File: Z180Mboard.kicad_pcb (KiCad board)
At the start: 2 copper layers, 170.2 x 170.2 mm, 66 parts, among them J1 Conn_02x05_Odd_Even, J10 PS2-MINIDIN6-FEMALE-SINGLE, J11 Conn_02x04_Odd_Even, J12 Conn_01x06, J13 Conn_01x06, J14 Conn_02x10_Top_Bottom, J15 Conn_02x05_Odd_Even, J16 DB9_Female, J17 Conn_01x40, J2 Conn_02x05_Odd_Even, J3 Conn_02x05_Odd_Even, J4 Conn_02x05_Odd_Even, J5 Conn_02x05_Odd_Even, J6 Conn_02x05_Odd_Even, J7 Conn_02x05_Odd_Even, J8 Conn_01x08, J9 PS2-MINIDIN6-FEMALE-SINGLE, SW1 SW_SPST, SW2 SW_Push, U1 Z8-L180-S180-180-PLCC-68, U10 74LVC245, U11 DS1307+, U2 SST39SF040, U3 74AHCT138, U4 74AHCT139, U5 AS6C4008-55PCN, U6 AS6C4008-55PCN, U7 82C55A_PLCC, U8 74HCT138, U9 74AHCT151, X1 CXO_DIP8, Y1 Crystal

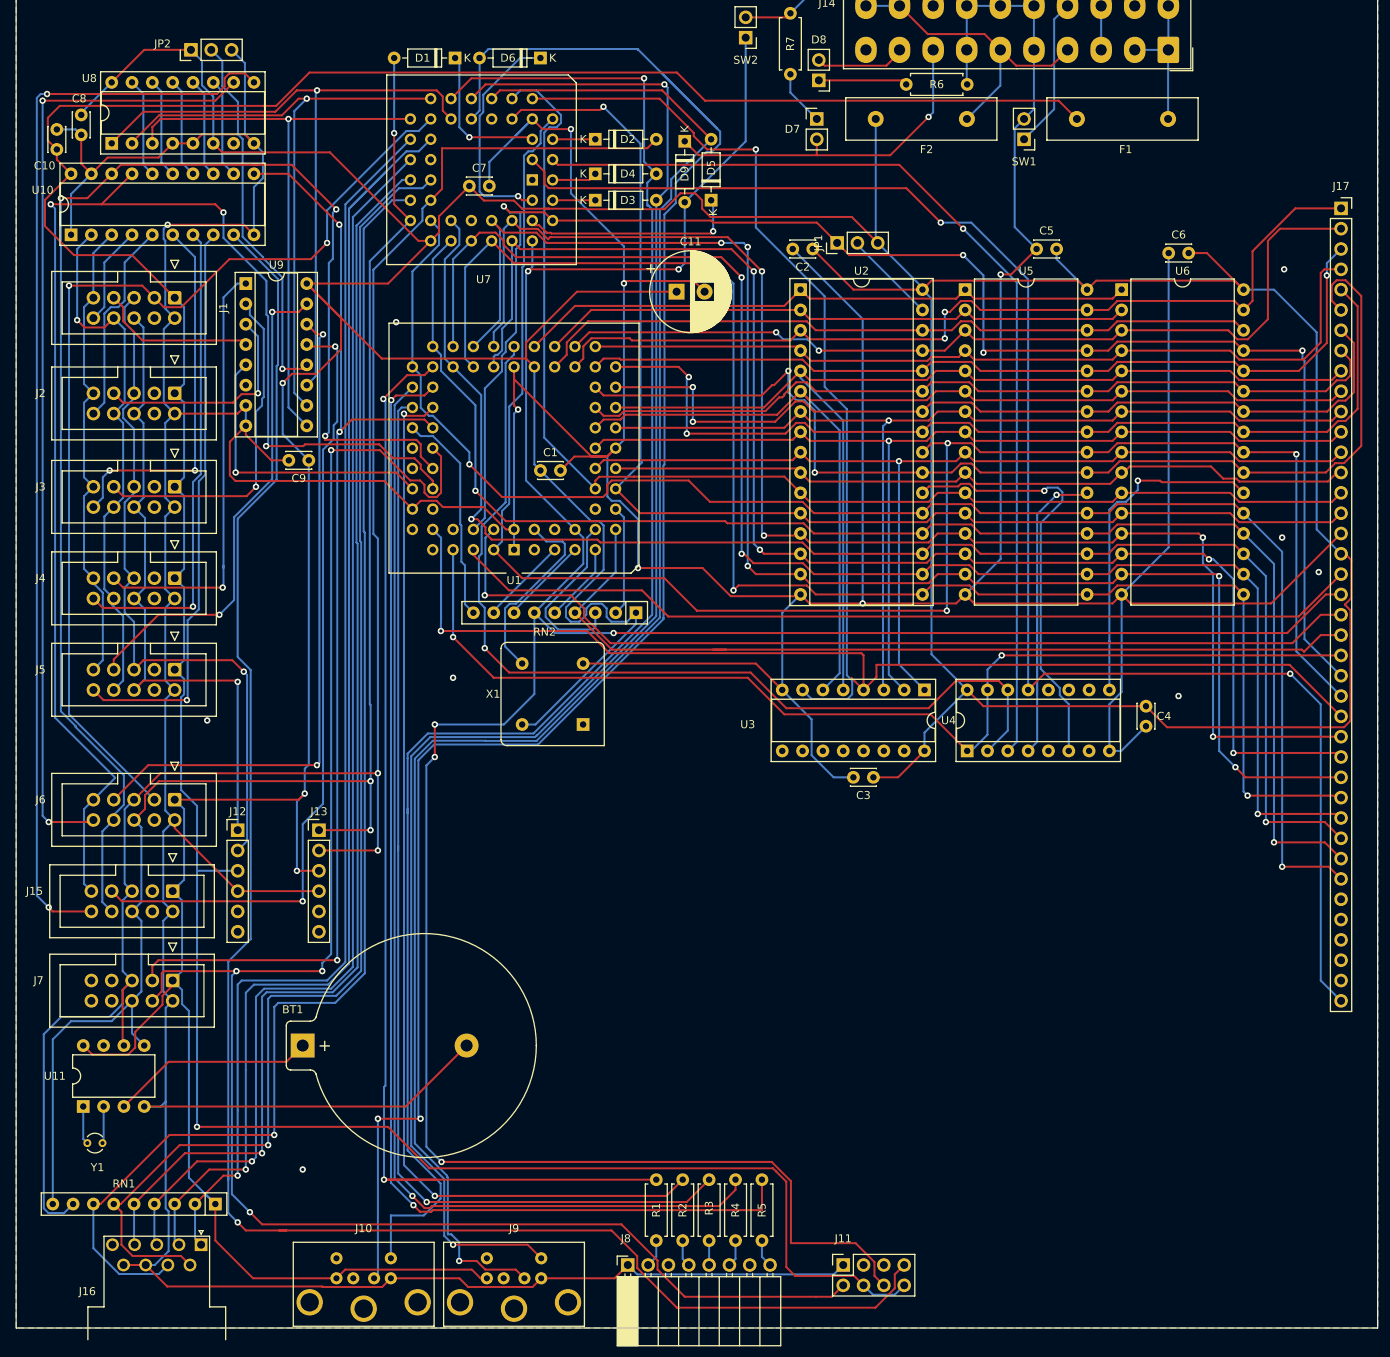
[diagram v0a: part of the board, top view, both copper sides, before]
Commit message: z180mboard: Add the floppy disk interface
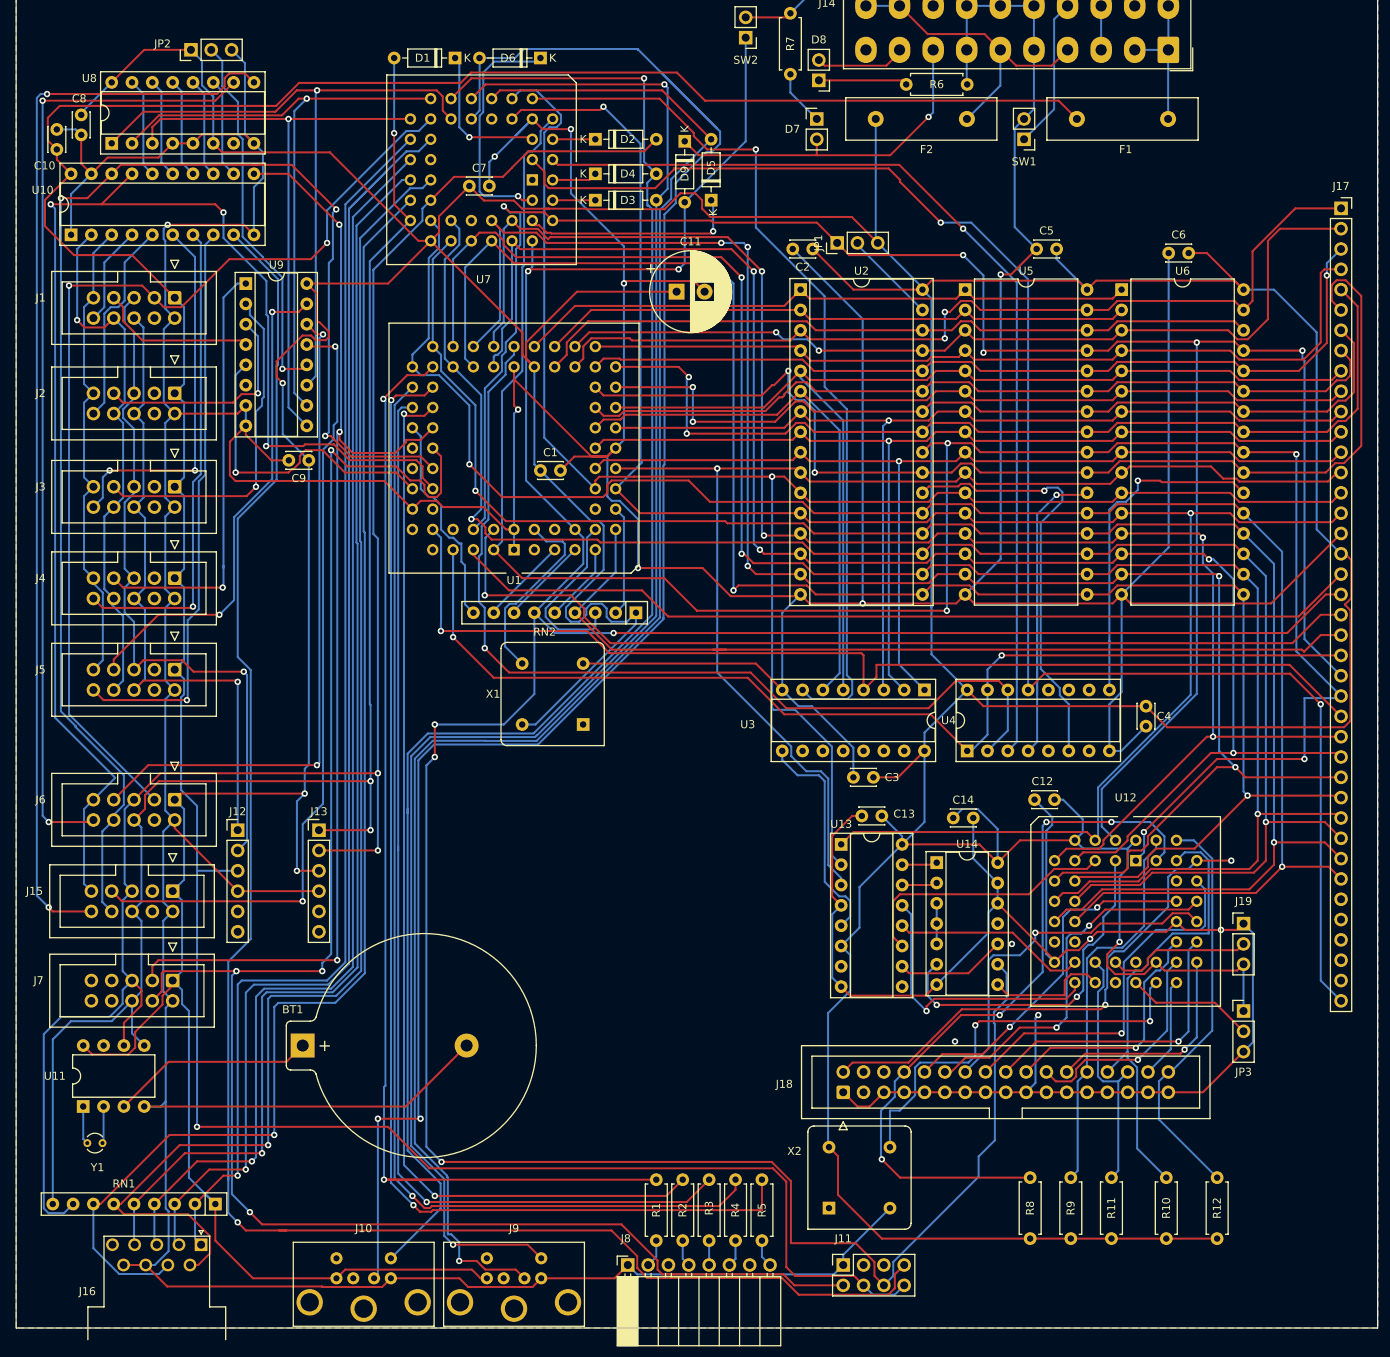
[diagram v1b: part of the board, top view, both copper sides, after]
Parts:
- added C12: 0.1uF, Capacitor_THT:C_Disc_D3.0mm_W2.0mm_P2.50mm, F.Cu at (177.5, 129.3)
- added C13: 0.1uF, Capacitor_THT:C_Disc_D3.0mm_W2.0mm_P2.50mm, F.Cu at (156.0, 131.3)
- added C14: 0.1uF, Capacitor_THT:C_Disc_D3.0mm_W2.0mm_P2.50mm, F.Cu at (164.9, 131.6)
- added J18: Conn_02x17_Odd_Even, Connector_IDC:IDC-Header_2x17_P2.54mm_Vertical, F.Cu at (151.1, 165.9)
- added J19: Conn_01x03, Connector_PinHeader_2.54mm:PinHeader_1x03_P2.54mm_Vertical, F.Cu at (201.2, 144.8)
- added JP3: Jumper_3_Open, Connector_PinHeader_2.54mm:PinHeader_1x03_P2.54mm_Vertical, F.Cu at (201.2, 155.7)
- added R10: 1K, Resistor_THT:R_Axial_DIN0207_L6.3mm_D2.5mm_P7.62mm_Horizontal, F.Cu at (191.5, 184.2)
- added R11: 1K, Resistor_THT:R_Axial_DIN0207_L6.3mm_D2.5mm_P7.62mm_Horizontal, F.Cu at (184.7, 184.2)
- added R12: 1K, Resistor_THT:R_Axial_DIN0207_L6.3mm_D2.5mm_P7.62mm_Horizontal, F.Cu at (197.9, 184.2)
- added R8: 1K, Resistor_THT:R_Axial_DIN0207_L6.3mm_D2.5mm_P7.62mm_Horizontal, F.Cu at (174.5, 184.2)
- added R9: 1K, Resistor_THT:R_Axial_DIN0207_L6.3mm_D2.5mm_P7.62mm_Horizontal, F.Cu at (179.6, 184.2)
- added U12: WD37C65C-DIP44, Package_LCC:PLCC-44_THT-Socket, F.Cu at (187.7, 136.9)
- added U13: 74HCT138, Package_DIP:DIP-16_W7.62mm_Socket, F.Cu at (150.9, 134.9)
- added U14: 74HCT00, Package_DIP:DIP-14_W7.62mm_Socket, F.Cu at (162.8, 137.2)
- added X2: CXO_DIP8, Oscillator:Oscillator_DIP-8, F.Cu at (149.4, 180.3)
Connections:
- U3 pad 9: (no net) -> FDCEN
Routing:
- net GND: track 1000.1 -> 1212.2 mm, vias 15 -> 13
- net VCC: track 769.7 -> 967.7 mm, vias 3 -> 4
- net INDEX: track 0.00 -> 92.3 mm, vias 0 -> 4
- net A0: track 157.9 -> 236.6 mm, vias 1 -> 2
- net WR: track 201.2 -> 269.1 mm, vias 4 -> 5
- net REDWC: track 0.00 -> 65.3 mm, vias 0 -> 2
- net A2: track 94.6 -> 154.1 mm, vias 0 -> 1
- net WPT: track 0.00 -> 57.4 mm
- net A1: track 156.7 -> 210.3 mm, vias 0 -> 1
- net DSKCHG: track 0.00 -> 51.2 mm
- net FDCLK: track 0.00 -> 51.1 mm, vias 0 -> 2
- net TRK00: track 0.00 -> 48.4 mm
- net RESET: track 355.4 -> 402.5 mm
- net DRVSB: track 0.00 -> 46.2 mm, vias 0 -> 2
- net MOTEB: track 0.00 -> 46.1 mm, vias 0 -> 1
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
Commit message: z180mboard: pack things in more tightly, turn the battery vertical
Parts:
- added U15: EF9345, Package_DIP:DIP-40_W15.24mm, F.Cu at (97.1, -92.9)
- BT1: footprint Battery:BatteryHolder_Keystone_106_1x20mm -> Battery:Battery_Panasonic_CR2032-VS1N_Vertical_CircularHoles
- moved BT1 15.3 mm to (68.8, 164.1), turned to 270 degrees
- moved RN1 1.27 mm to (72.6, 181.1)
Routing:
- net GND: track 1212.2 -> 1174.0 mm, vias 13 -> 16
- net CSEL1: track 79.4 -> 64.0 mm
- net Net-(BT1-Pad1): track 25.5 -> 10.7 mm
- net Net-(JP2-Pad2): track 46.8 -> 41.9 mm
- net FIRE: track 176.2 -> 172.3 mm
- net CS6: track 136.8 -> 134.0 mm
- net SCL_IN: track 230.0 -> 232.2 mm
- net 3V3: track 387.8 -> 386.3 mm
- net SDA_IN: track 201.7 -> 203.0 mm
- net VCC: track 967.7 -> 966.6 mm
- net UP: track 156.9 -> 158.0 mm
- net LEFT: track 157.9 -> 157.2 mm
- net FIRE2: track 171.0 -> 170.5 mm

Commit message: z180mboard; Add video, holes tidy stuff up
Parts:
- added C15: 0.1uF, Capacitor_THT:C_Disc_D3.0mm_W2.0mm_P2.50mm, F.Cu at (126.2, 128.0)
- added C16: 0.1nF, Capacitor_THT:C_Disc_D3.0mm_W2.0mm_P2.50mm, F.Cu at (102.4, 149.4)
- added C17: C, Capacitor_THT:C_Disc_D3.0mm_W2.0mm_P2.50mm, F.Cu at (128.8, 142.7)
- added C18: C, Capacitor_THT:C_Disc_D3.0mm_W2.0mm_P2.50mm, F.Cu at (128.8, 136.1)
- added J20: Conn_01x06, Connector_PinSocket_2.54mm:PinSocket_1x06_P2.54mm_Vertical, F.Cu at (139.2, 164.3)
- added J21: Conn_01x06, Connector_PinHeader_2.54mm:PinHeader_1x06_P2.54mm_Vertical, F.Cu at (186.4, 192.3)
- added J22: Conn_Coaxial, Connector_Coaxial:BNC_Amphenol_B6252HB-NPP3G-50_Horizontal, F.Cu at (174.0, 183.1)
- added J23: Conn_01x05, Connector_PinHeader_2.54mm:PinHeader_1x05_P2.54mm_Vertical, F.Cu at (113.0, 170.4)
- added JP4: Jumper_3_Open, Connector_PinHeader_2.54mm:PinHeader_1x03_P2.54mm_Vertical, F.Cu at (102.1, 133.1)
- added R13: 47K, Resistor_THT:R_Axial_DIN0207_L6.3mm_D2.5mm_P7.62mm_Horizontal, F.Cu at (123.7, 148.3)
- added R14: 810, Resistor_THT:R_Axial_DIN0207_L6.3mm_D2.5mm_P7.62mm_Horizontal, F.Cu at (185.7, 172.0)
- added R15: 220, Resistor_THT:R_Axial_DIN0207_L6.3mm_D2.5mm_P7.62mm_Horizontal, F.Cu at (200.9, 189.0)
- added R16: 220, Resistor_THT:R_Axial_DIN0207_L6.3mm_D2.5mm_P7.62mm_Horizontal, F.Cu at (197.6, 189.0)
- added R17: 220, Resistor_THT:R_Axial_DIN0207_L6.3mm_D2.5mm_P7.62mm_Horizontal, F.Cu at (194.3, 189.0)
- added R18: 270, Resistor_THT:R_Axial_DIN0207_L6.3mm_D2.5mm_P7.62mm_Horizontal, F.Cu at (191.0, 181.4)
- added R19: 100, Resistor_THT:R_Axial_DIN0207_L6.3mm_D2.5mm_P7.62mm_Horizontal, F.Cu at (185.9, 178.8)
- added RV1: R_POT, Potentiometer_THT:Potentiometer_Vishay_T7-YA_Single_Vertical, F.Cu at (180.1, 176.5)
- added Y2: 13.875MHz, Crystal:Crystal_C26-LF_D2.1mm_L6.5mm_Vertical, F.Cu at (124.2, 140.5)
- U15: value EF9345 -> STV5348; footprint Package_DIP:DIP-40_W15.24mm -> Package_DIP:DIP-28_W15.24mm
- moved U15 221.1 mm to (105.7, 128.0)
- moved R12 32.2 mm to (204.7, 152.7), turned to 270 degrees
- moved R10 19.5 mm to (172.7, 178.8)
- moved R11 16.1 mm to (169.4, 178.8)
- moved R9 14.7 mm to (165.9, 178.8)
- moved R8 13.8 mm to (161.8, 178.8)
- moved U11 7.84 mm to (52.8, 174.8)
- moved Y1 5.91 mm to (54.1, 177.5)
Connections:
- U15 pad 10: (no net) -> B
- U15 pad 11: (no net) -> VCC
- U15 pad 16: (no net) -> SCL_IN
- U15 pad 17: (no net) -> SDA_IN
- U15 pad 2: (no net) -> GND
- U15 pad 20: (no net) -> Net-(R13-Pad1)
- U15 pad 21: (no net) -> GND
- U15 pad 22: (no net) -> VCC
- U15 pad 23: (no net) -> Net-(C17-Pad2)
- U15 pad 24: (no net) -> Net-(C18-Pad2)
- U15 pad 25: (no net) -> GND
- U15 pad 26: (no net) -> GND
- U15 pad 27: (no net) -> GND
- U15 pad 28: (no net) -> Net-(C15-Pad1)
- U15 pad 3: (no net) -> VCC
- U15 pad 4: (no net) -> Net-(JP4-Pad2)
- U15 pad 5: (no net) -> CSYNC
- U15 pad 7: (no net) -> GND
- U15 pad 8: (no net) -> R
- U15 pad 9: (no net) -> G
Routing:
- net GND: track 1174.0 -> 1389.0 mm, vias 16 -> 35
- net R: track 0.00 -> 129.3 mm
- net G: track 0.00 -> 123.3 mm
- net CSYNC: track 0.00 -> 122.3 mm
- net B: track 0.00 -> 113.8 mm
- net VCC: track 966.6 -> 1037.5 mm
- net SDA_IN: track 203.0 -> 272.3 mm, vias 3 -> 4
- net SCL_IN: track 232.2 -> 295.5 mm, vias 2 -> 3
- net Net-(J22-Pad1): track 0.00 -> 34.5 mm
- net TX_0: track 140.0 -> 158.2 mm
- net Net-(R19-Pad1): track 0.00 -> 17.8 mm
- net CSEL1: track 64.0 -> 79.4 mm
- net CTS_0: track 146.2 -> 159.0 mm
- net RX_0: track 135.5 -> 148.2 mm
- net RESET: track 402.5 -> 415.1 mm, vias 6 -> 7
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
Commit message: Z180Mboard: more cleaning up and connector add
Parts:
- added J24: Conn_01x15, Connector_PinSocket_2.54mm:PinSocket_1x15_P2.54mm_Vertical, F.Cu at (135.4, 118.9)
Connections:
- J1 pad 4: (no net) -> Net-(J1-Pad4)
- J10 pad 2: (no net) -> Net-(J10-Pad2)
- J10 pad 6: (no net) -> Net-(J10-Pad6)
- J11 pad 3: (no net) -> Net-(J11-Pad3)
- J11 pad 5: (no net) -> Net-(J11-Pad5)
- J12 pad 5: (no net) -> Net-(J12-Pad5)
- J12 pad 6: (no net) -> Net-(J12-Pad6)
- J13 pad 5: (no net) -> Net-(J13-Pad5)
- J13 pad 6: (no net) -> Net-(J13-Pad6)
- J14 pad 10: (no net) -> Net-(J14-Pad10)
- J14 pad 12: (no net) -> Net-(J14-Pad12)
- J14 pad 18: (no net) -> Net-(J14-Pad18)
- J15 pad 3: (no net) -> Net-(J15-Pad3)
- J15 pad 4: (no net) -> Net-(J15-Pad4)
- J16 pad 5: (no net) -> Net-(J16-Pad5)
- J17 pad 35: (no net) -> Net-(J17-Pad35)
- J17 pad 36: (no net) -> Net-(J17-Pad36)
- J17 pad 37: (no net) -> Net-(J17-Pad37)
- J17 pad 38: (no net) -> Net-(J17-Pad38)
- J17 pad 39: (no net) -> Net-(J17-Pad39)
- J18 pad 3: (no net) -> Net-(J18-Pad3)
- J18 pad 4: (no net) -> Net-(J18-Pad4)
- J18 pad 6: (no net) -> Net-(J18-Pad6)
- J2 pad 3: (no net) -> Net-(J2-Pad3)
- J2 pad 4: (no net) -> Net-(J2-Pad4)
- J3 pad 3: (no net) -> Net-(J3-Pad3)
- J3 pad 4: (no net) -> Net-(J3-Pad4)
- J4 pad 3: (no net) -> Net-(J4-Pad3)
- J4 pad 4: (no net) -> Net-(J4-Pad4)
- J5 pad 3: (no net) -> Net-(J5-Pad3)
- J5 pad 4: (no net) -> Net-(J5-Pad4)
- J6 pad 4: (no net) -> Net-(J6-Pad4)
- J7 pad 10: (no net) -> Net-(J7-Pad10)
- J7 pad 7: (no net) -> Net-(J7-Pad7)
- J7 pad 8: (no net) -> Net-(J7-Pad8)
- J7 pad 9: (no net) -> Net-(J7-Pad9)
- J8 pad 3: (no net) -> Net-(J8-Pad3)
- J8 pad 7: (no net) -> Net-(J8-Pad7)
- J9 pad 2: (no net) -> Net-(J9-Pad2)
- J9 pad 6: (no net) -> Net-(J9-Pad6)
- RV1 pad 1: (no net) -> Net-(RV1-Pad1)
- U1 pad 13: (no net) -> Net-(U1-Pad13)
- U1 pad 3: (no net) -> Net-(U1-Pad3)
- U1 pad 52: (no net) -> Net-(U1-Pad52)
- U1 pad 54: (no net) -> Net-(U1-Pad54)
- U1 pad 59: (no net) -> Net-(U1-Pad59)
- U1 pad 6: (no net) -> Net-(U1-Pad6)
- U1 pad 60: (no net) -> Net-(U1-Pad60)
- U1 pad 61: (no net) -> Net-(U1-Pad61)
- U1 pad 64: (no net) -> Net-(U1-Pad64)
- U11 pad 7: (no net) -> Net-(U11-Pad7)
- U12 pad 15: (no net) -> Net-(U12-Pad15)
- U12 pad 16: (no net) -> Net-(U12-Pad16)
- U12 pad 22: (no net) -> Net-(U12-Pad22)
- U12 pad 25: (no net) -> Net-(U12-Pad25)
- U12 pad 38: (no net) -> Net-(U12-Pad38)
- U13 pad 7: (no net) -> Net-(U13-Pad7)
- U13 pad 9: (no net) -> Net-(U13-Pad9)
- U14 pad 11: (no net) -> Net-(U14-Pad11)
- U15 pad 1: (no net) -> Net-(U15-Pad1)
- U15 pad 12: (no net) -> Net-(U15-Pad12)
- U15 pad 13: (no net) -> Net-(U15-Pad13)
- U15 pad 14: (no net) -> Net-(U15-Pad14)
- U15 pad 15: (no net) -> Net-(U15-Pad15)
- U15 pad 18: (no net) -> Net-(U15-Pad18)
- U15 pad 19: (no net) -> Net-(U15-Pad19)
- U15 pad 6: (no net) -> Net-(U15-Pad6)
- U3 pad 10: (no net) -> Net-(U3-Pad10)
- U3 pad 11: (no net) -> Net-(U3-Pad11)
- U3 pad 12: (no net) -> Net-(U3-Pad12)
- U3 pad 13: (no net) -> Net-(U3-Pad13)
- U3 pad 14: (no net) -> Net-(U3-Pad14)
- U3 pad 15: (no net) -> Net-(U3-Pad15)
- U4 pad 10: (no net) -> Net-(U4-Pad10)
- U4 pad 11: (no net) -> Net-(U4-Pad11)
- U4 pad 12: (no net) -> Net-(U4-Pad12)
- U4 pad 5: (no net) -> Net-(U4-Pad5)
- U4 pad 7: (no net) -> Net-(U4-Pad7)
- U7 pad 1: (no net) -> Net-(U7-Pad1)
- U7 pad 12: (no net) -> Net-(U7-Pad12)
- U7 pad 23: (no net) -> Net-(U7-Pad23)
- U7 pad 34: (no net) -> Net-(U7-Pad34)
- U8 pad 7: (no net) -> Net-(U8-Pad7)
- U9 pad 6: (no net) -> Net-(U9-Pad6)
- X1 pad 1: (no net) -> Net-(X1-Pad1)
- X2 pad 1: (no net) -> Net-(X2-Pad1)
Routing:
- net 3V3: track 386.3 -> 646.3 mm, vias 1 -> 3
- net EXTMEM: track 199.8 -> 253.7 mm, vias 2 -> 3
- net VCC: track 1037.5 -> 1090.1 mm
- net SCL_IN: track 295.5 -> 335.0 mm
- net SDA_IN: track 272.3 -> 306.6 mm
- net GND: track 1389.0 -> 1416.1 mm, vias 35 -> 38
- net M1: track 114.8 -> 123.6 mm
- net RD: track 259.4 -> 267.5 mm
- net MSDATA_IN: track 227.5 -> 221.3 mm
- net REDWC: track 65.3 -> 67.8 mm
- net B: track 113.8 -> 115.4 mm
- net RESET: track 415.1 -> 416.6 mm
- net IORQ: track 146.5 -> 148.0 mm
- net A2: track 154.1 -> 155.0 mm
- net FDCEN: track 27.8 -> 28.6 mm
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
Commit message: Notes for bugs/mods for v2/v3
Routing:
- net VCC: track 1090.1 -> 1285.1 mm
- net 3V3: track 646.3 -> 765.3 mm
- net GND: track 1416.1 -> 1446.4 mm, vias 38 -> 46
- net VCC_UF: track 39.5 -> 66.7 mm
- net 3V3_UF: track 18.3 -> 32.5 mm
- net MISO4: track 62.1 -> 70.1 mm
- net CS4_3: track 72.0 -> 78.7 mm
- net TX_1_3: track 222.0 -> 227.0 mm
- net CS3_3: track 60.3 -> 64.1 mm
- net CS2_3: track 46.7 -> 49.4 mm
- net B: track 115.4 -> 117.6 mm
